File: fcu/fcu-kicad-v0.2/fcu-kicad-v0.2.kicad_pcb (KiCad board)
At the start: 2 copper layers, 133.9 x 50.8 mm, 189 parts, among them J1 Conn_01x02, J10 Conn_01x02_Socket, J11 Conn_01x04_Socket, J12 Conn_01x02_Socket, J13 Conn_01x02_Socket, J14 Conn_01x02_Socket, J15 Conn_01x02_Socket, J16 Conn_01x02_Socket, J17 Conn_01x02_Socket, J18 Conn_01x02_Socket, J19 Conn_01x02_Socket, J2 Conn_01x04_Socket, J20 Conn_01x02_Socket, J21 Conn_01x02_Socket, J22 Conn_01x02_Socket, J23 Conn_01x02_Socket, J24 Conn_01x02_Socket, J25 Conn_01x02, J3 Conn_01x01, J4 Conn_01x02_Socket, J5 Conn_01x03_Pin, J6 Conn_01x04_Socket, J7 Conn_01x06_Socket, J8 Conn_01x03_Socket, J9 Conn_01x02_Socket, SW1 SW_RST, U1 MCP1416, U10 RQ3E100, U11 RQ3E100, U12 MS5611-01BA, U13 W25X05, U14 W25X05, U15 LAN8742, U16 MCP1416, U17 MAX-8C, U18 RQ3E100, U19 AP62300TWU, U2 MCP1416, U20 LD39200, U21 TXB0108DQSR, U3 RQ3E100, U4 RQ3E100, U5 STM32F407VGTx, U6 MCP1416, U7 MCP1416, U8 BMM150, U9 BMI088, Y1 25 MHz, Y2 25 MHz

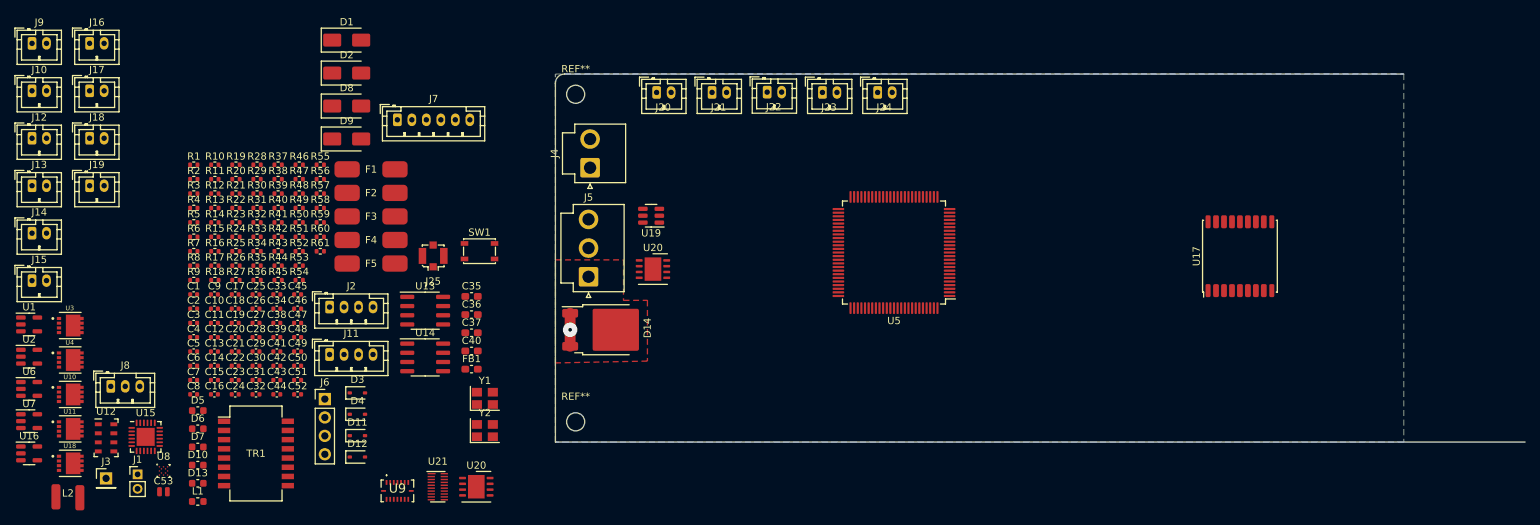
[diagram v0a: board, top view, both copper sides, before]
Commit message: Routing work on FCU v0.2
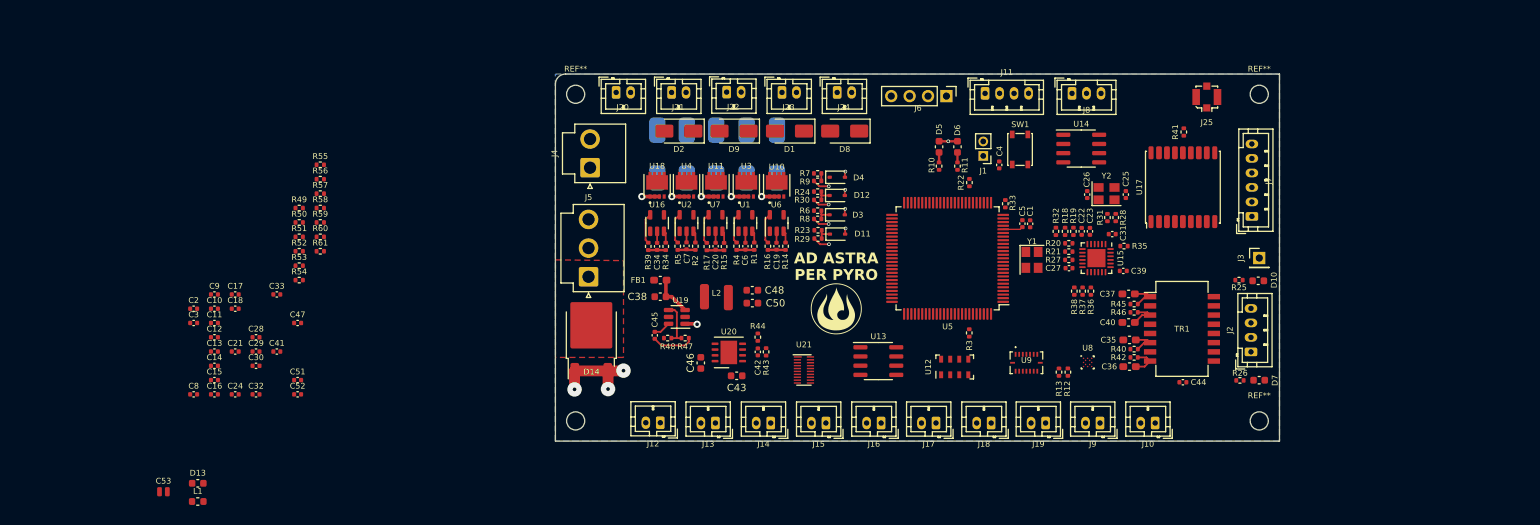
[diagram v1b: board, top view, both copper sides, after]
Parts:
- removed C49: 10uF, Capacitor_SMD:C_0402_1005Metric
- removed the U20 at (115.1, 89.9)
- added G***: LOGO, CustomFootprints:Logo, F.Cu at (140.4, 95.4)
- added REF**: MountingHole_2.5mm, MountingHole:MountingHole_2.5mm, F.Cu at (198.8, 65.8)
- added REF**: MountingHole_2.5mm, MountingHole:MountingHole_2.5mm, F.Cu at (198.8, 110.9)
- C38, C43, C46, C48, C50: footprint Capacitor_SMD:C_0402_1005Metric -> Capacitor_SMD:C_0603_1608Metric
- F1, F2, F3, F4, F5: moved to B.Cu
- moved J3 162.1 mm to (198.8, 88.4)
- moved J10 161.7 mm to (184.4, 111.2), turned to 180 degrees
- moved J9 156.5 mm to (176.8, 111.2), turned to 180 degrees
- moved D10 148.6 mm to (198.6, 91.5), turned to 180 degrees
- moved D7 146.8 mm to (198.7, 105.3), turned to 180 degrees
- moved R26 139.5 mm to (196.1, 105.3)
- moved J8 138.7 mm to (172.9, 65.7)
- moved R25 138.5 mm to (196.0, 91.4), turned to 180 degrees
- moved J19 136.0 mm to (169.3, 111.2), turned to 180 degrees
- moved U15 133.5 mm to (176.3, 88.4), turned to -90 degrees
- moved J18 130.5 mm to (161.8, 111.2), turned to 180 degrees
- moved TR1 129.0 mm to (188.1, 98.2)
- moved U8 128.4 mm to (175.1, 102.8)
- moved J2 127.3 mm to (197.6, 101.3), turned to 90 degrees
- moved R41 125.6 mm to (188.3, 71.0), turned to 90 degrees
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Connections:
- J4 pad 1: Vdrive -> Net-(J4-Pin_1)
- J4 pad 2: Net-(J4-Pin_2) -> Vdrive
- J5 pad 3: Net-(J4-Pin_2) -> Net-(J4-Pin_1)
- R54 pad 1: Net-(J4-Pin_2) -> Net-(J4-Pin_1)
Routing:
- net GND: track 4.56 -> 52.7 mm, vias 1 -> 18
- net +12V: track 0.00 -> 7.90 mm
- net Net-(U19-FB): track 0.00 -> 6.22 mm
- net Net-(U19-SW): track 0.00 -> 5.82 mm
- net Net-(U19-IN): track 0.00 -> 5.73 mm
- net /DRX-: track 0.00 -> 4.38 mm
- net /DRX+: track 0.00 -> 4.38 mm
- net Net-(U11-Gate): track 0.00 -> 4.29 mm
- net Net-(U16-OUT): track 0.00 -> 4.27 mm
- net Net-(U1-OUT): track 0.00 -> 4.25 mm
- net Net-(U2-OUT): track 0.00 -> 4.23 mm
- net Net-(U10-Gate): track 0.00 -> 4.23 mm
- net /DTX-: track 0.00 -> 4.20 mm
- net /DTX+: track 0.00 -> 4.20 mm
- net +3.3V: track 0.00 -> 2.78 mm
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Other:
- board size 133.9 x 50.8 mm -> 99.9 x 50.7 mm

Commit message: FCU PCB Work
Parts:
- moved C47 128.2 mm to (193.9, 88.4)
- moved R49 125.5 mm to (191.5, 89.0)
- moved R50 125.4 mm to (191.5, 87.8)
- moved C3 119.2 mm to (170.7, 91.2), turned to 180 degrees
- moved C2 119.0 mm to (170.7, 96.8)
- moved C12 114.2 mm to (168.0, 87.0), turned to -90 degrees
- moved C17 111.6 mm to (168.2, 79.6)
- moved C18 111.6 mm to (168.2, 81.6)
- moved C10 111.2 mm to (165.7, 92.6), turned to 180 degrees
- moved C11 111.0 mm to (165.2, 89.7), turned to 90 degrees
- moved R59 108.5 mm to (176.3, 100.6), turned to -90 degrees
- moved R58 106.7 mm to (173.5, 103.9), turned to 90 degrees
- moved C8 102.7 mm to (150.2, 78.5), turned to -90 degrees
- moved R57 102.1 mm to (167.6, 106.3), turned to -90 degrees
- moved R56 100.2 mm to (165.1, 106.3), turned to -90 degrees
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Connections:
- Y1 pad 2: Net-(U5-PH0) -> GND
- Y1 pad 3: (no net) -> Net-(U5-PH0)
- Y1 pad 4: (no net) -> GND
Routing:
- net +3.3V: track 2.78 -> 7.76 mm
- net Earth: track 0.00 -> 4.35 mm
- net GND: track 52.7 -> 56.6 mm
- net Net-(C47-Pad1): track 0.00 -> 3.37 mm
- net Net-(D13-A): track 0.00 -> 2.64 mm
- net Net-(U5-VCAP_2): track 0.00 -> 1.85 mm
- net Net-(U5-PH0): track 0.00 -> 1.85 mm
- net Net-(U5-PH1): track 0.00 -> 1.85 mm
- net Net-(U5-VCAP_1): track 0.00 -> 1.79 mm
- net Net-(U9-SDO2): track 0.00 -> 1.79 mm
- net Net-(U9-SDO1): track 0.00 -> 1.78 mm
- net Net-(U21-A7): track 0.00 -> 1.77 mm
- net Net-(U21-A8): track 0.00 -> 1.59 mm
- net ADC1_IN9: track 0.00 -> 1.14 mm
- net ADC1_IN10: track 0.00 -> 1.14 mm

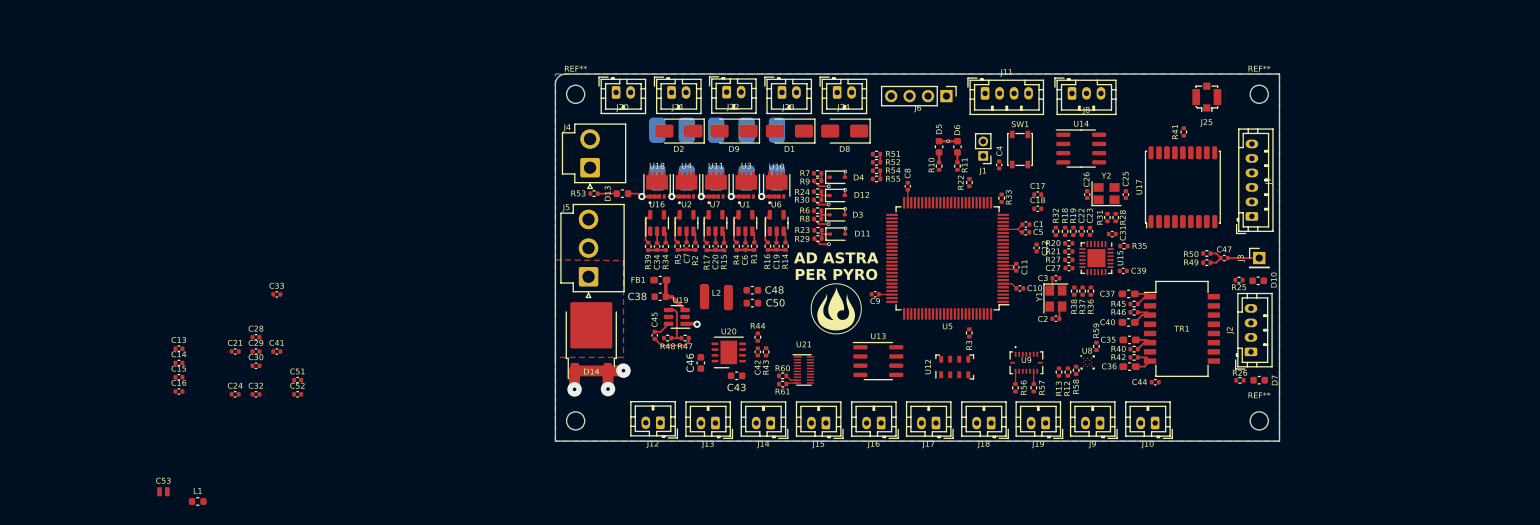
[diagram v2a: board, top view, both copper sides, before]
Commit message: mission-control-ui rocket page + FCU simulation
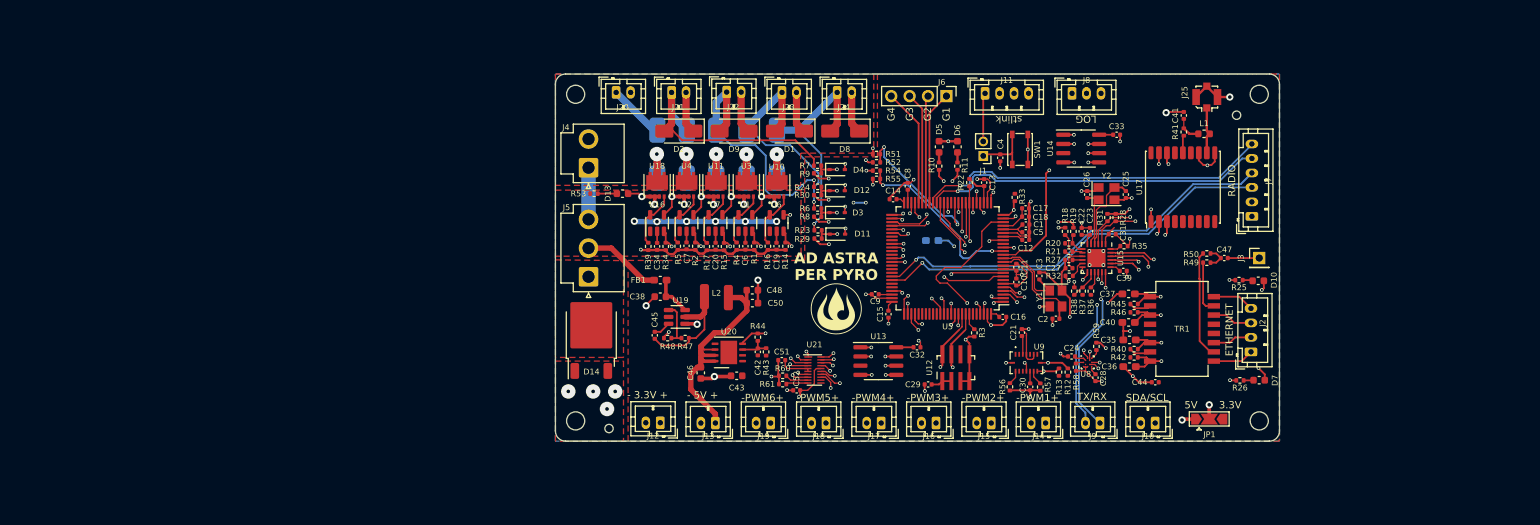
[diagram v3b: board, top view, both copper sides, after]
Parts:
- added JP1: SolderJumper_3_Open, Jumper:SolderJumper-3_P2.0mm_Open_TrianglePad1.0x1.5mm, F.Cu at (191.8, 110.6)
- added REF**: JLCPCB_ToolingHole, CustomFootprints:JLCPCB_ToolingHole, F.Cu at (109.0, 111.9)
- added REF**: JLCPCB_ToolingHole, CustomFootprints:JLCPCB_ToolingHole, F.Cu at (195.6, 68.7)
- C53: footprint Capacitor_SMD:C_0504_1310Metric -> Capacitor_SMD:C_0603_1608Metric_Pad1.08x0.95mm_HandSolder; moved to B.Cu
- R52: value 21K -> 10K
- R53: value 2K -> 2.4K
- R54: value 21K -> 20K
- U12: footprint Package_LGA:LGA-8_3x5mm_P1.25mm -> CustomFootprints:LGA-8_3x5mm_P1.25mm_HandSolder
- moved L1 147.9 mm to (191.1, 71.2)
- moved C41 129.4 mm to (188.3, 68.7), turned to 90 degrees
- moved C33 118.0 mm to (179.1, 71.4), turned to 180 degrees
- moved C28 116.0 mm to (176.1, 104.9), turned to -90 degrees
- moved C24 115.6 mm to (172.8, 102.0)
- moved C16 114.2 mm to (163.3, 96.5), turned to 180 degrees
- moved C13 113.5 mm to (160.8, 78.0), turned to -90 degrees
- moved C53 111.6 mm to (153.6, 86.0)
- moved C21 108.6 mm to (166.0, 98.7), turned to 90 degrees
- moved C30 106.9 mm to (167.1, 106.2), turned to -90 degrees
- moved C14 101.1 mm to (148.2, 80.3)
- moved C15 98.3 mm to (147.6, 96.1), turned to 90 degrees
- moved C29 92.9 mm to (153.1, 105.8), turned to 180 degrees
- moved C32 91.5 mm to (151.5, 100.7), turned to 180 degrees
- moved C52 68.9 mm to (134.9, 106.7)
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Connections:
- J7 pad 1: +5V -> Net-(J7-Pin_1)
- Y2 pad 2: Net-(U15-XTAL2) -> GND
- Y2 pad 3: (no net) -> Net-(U15-XTAL2)
- Y2 pad 4: (no net) -> GND
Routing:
- net GND: track 56.6 -> 229.6 mm, vias 18 -> 79
- net +5V: track 0.00 -> 121.0 mm, vias 0 -> 2
- net I2C1_SCL: track 0.00 -> 85.3 mm, vias 0 -> 4
- net I2C1_SDA: track 0.00 -> 80.6 mm, vias 0 -> 4
- net +12V: track 7.90 -> 85.5 mm, vias 0 -> 7
- net TIM5_CH1: track 1.67 -> 66.5 mm, vias 0 -> 2
- net +3.3V: track 7.76 -> 65.4 mm, vias 0 -> 3
- net USART1_TX: track 0.00 -> 56.6 mm, vias 0 -> 1
- net USART1_RX: track 0.00 -> 55.7 mm, vias 0 -> 1
- net USART3_RX: track 0.00 -> 52.6 mm, vias 0 -> 2
- net USART3_TX: track 0.00 -> 51.2 mm, vias 0 -> 2
- net RADIO_RTS: track 0.00 -> 48.5 mm, vias 0 -> 1
- net RADIO_CTS: track 0.00 -> 47.4 mm, vias 0 -> 1
- net UART4_TX: track 0.00 -> 47.3 mm, vias 0 -> 2
- net Net-(J4-Pin_1): track 0.00 -> 46.6 mm, vias 0 -> 1
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- added copper zone on In1.Cu, net (none)
- added copper zone on In2.Cu, net (none)
- added copper zone on F.Cu, net +12V
- added copper zone on F.Cu, net +3.3V
- added copper zone on F.Cu, net GND
- added copper zone on F.Cu, net Vdrive
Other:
- outline, holes or cut-outs redrawn
- copper layers 2 -> 4
- board text added: "+12V"
- board text added: "+OUT1-"
- board text added: "+OUT2-"
- board text added: "+OUT3-"
- board text added: "+OUT4-"
- board text added: "+PIEZO-"
- board text added: "+Vdd"
- board text added: "- 3.3V +"
- board text added: "- 5V +"
- board text added: "-PWM1+"
- board text added: "-PWM2+"
- board text added: "-PWM3+"
- board text added: "-PWM4+"
- board text added: "-PWM5+"
- board text added: "-PWM6+"
- board text added: "3.3V"
- board text added: "5V"
- board text added: "CTS"
- board text added: "EARTH"
- board text added: "ETHERNET"
- board text added: "FCU v0.2"
- board text added: "G1"
- board text added: "G2"
- board text added: "G3"
- board text added: "G4"
- board text added: "GND"
- board text added: "JLCJLCJLCJLC"
- board text added: "LOG"
- board text added: "R+"
- board text added: "R-"
- board text added: "RADIO"
- board text added: "RTS"
- board text added: "RX"
- board text added: "SDA/SCL"
- board text added: "SWCLK"
- board text added: "SWDIO"
- board text added: "T+"
- board text added: "T-"
- board text added: "TX"
- board text added: "TX/RX"
- board text added: "Vcc"
- board text added: "stlink"
- board text added: "~{RST}"
